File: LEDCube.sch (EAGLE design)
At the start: 19 parts

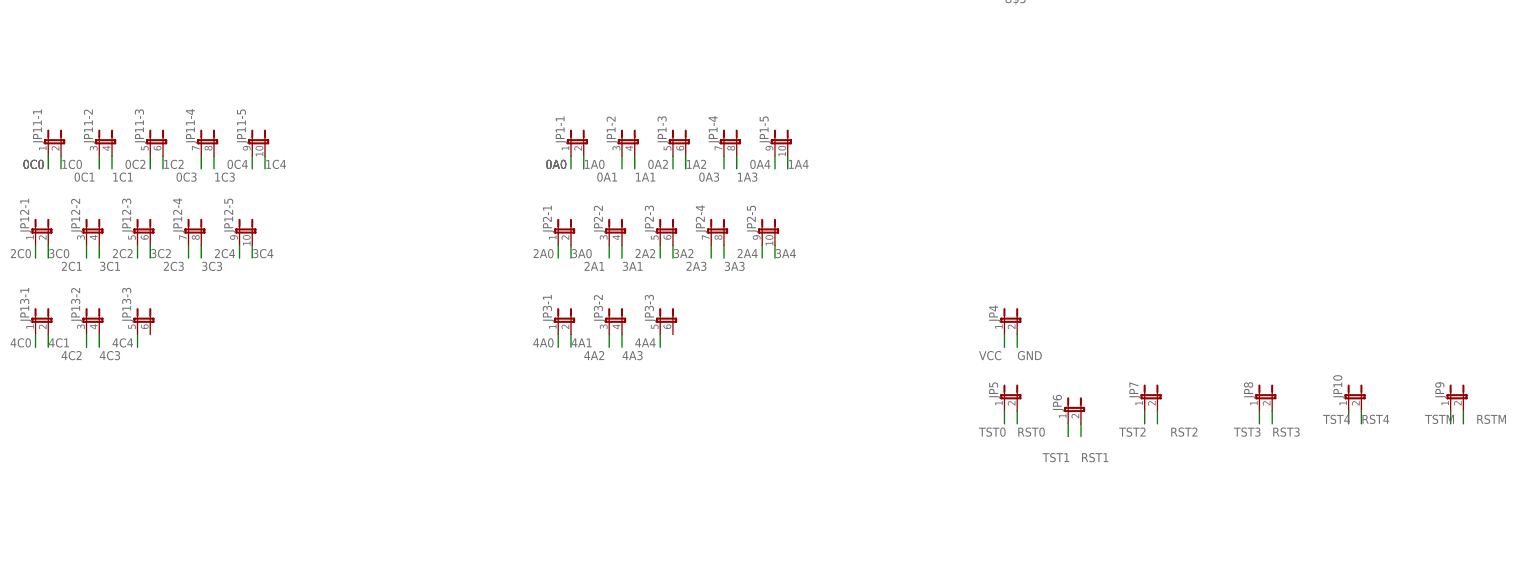
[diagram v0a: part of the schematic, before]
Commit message: Laid out MSP430 board. Not routed yet.
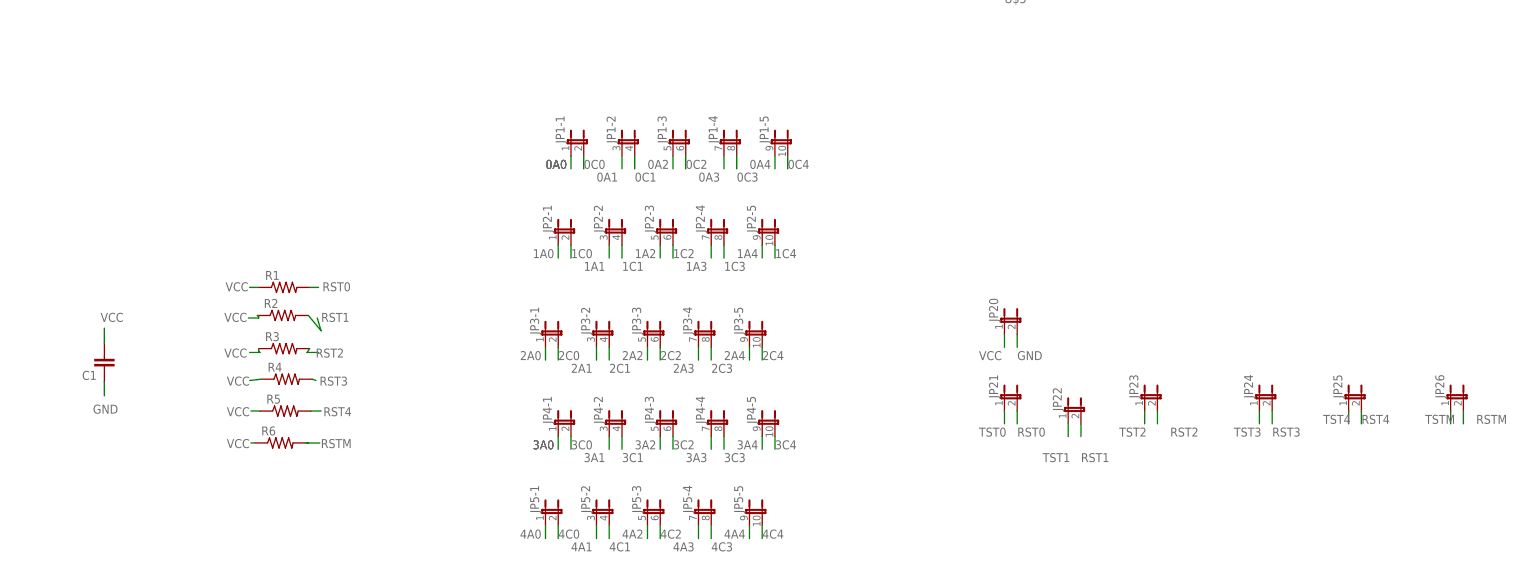
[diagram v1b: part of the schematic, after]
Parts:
- removed JP11, JP12, JP13: (no value), jumper:JP5QE
- added C1: (no value), eagle-ltspice:CC1206
- added JP20, JP21: (no value), jumper:JP1E
- added R1, R2, R3, R4, R5, R6: (no value), rcl:R-US_R1206
- JP4, JP5: device jumper:JP1E -> jumper:JP5QE
- renumbered JP10 to JP25, JP6 to JP22, JP7 to JP23, JP8 to JP24, JP9 to JP26
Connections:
- net 0C0: now also JP1-1.2; no longer JP11-1.1
- net 0C1: now also JP1-2.2; no longer JP11-2.1
- net 0C2: now also JP1-3.2; no longer JP11-3.1
- net 0C3: now also JP1-4.2; no longer JP11-4.1
- net 0C4: now also JP1-5.2; no longer JP11-5.1
- net 1A0: now also JP2-1.1; no longer JP1-1.2
- net 1A1: now also JP2-2.1; no longer JP1-2.2
- net 1A2: now also JP2-3.1; no longer JP1-3.2
- net 1A3: now also JP2-4.1; no longer JP1-4.2
- net 1A4: now also JP2-5.1; no longer JP1-5.2
- net 1C0: now also JP2-1.2; no longer JP11-1.2
- net 1C1: now also JP2-2.2; no longer JP11-2.2
- net 1C2: now also JP2-3.2; no longer JP11-3.2
- net 1C3: now also JP2-4.2; no longer JP11-4.2
- net 1C4: now also JP2-5.2; no longer JP11-5.2
- net 2A0: now also JP3-1.1; no longer JP2-1.1
- net 2A1: now also JP3-2.1; no longer JP2-2.1
- net 2A2: now also JP3-3.1; no longer JP2-3.1
- net 2A3: now also JP3-4.1; no longer JP2-4.1
- net 2A4: now also JP3-5.1; no longer JP2-5.1
- net 2C0: now also JP3-1.2; no longer JP12-1.1
- net 2C1: now also JP3-2.2; no longer JP12-2.1
- net 2C2: now also JP3-3.2; no longer JP12-3.1
- net 2C3: now also JP3-4.2; no longer JP12-4.1
- net 2C4: now also JP3-5.2; no longer JP12-5.1
- net 3A0: now also JP4-1.1; no longer JP2-1.2
- net 3A1: now also JP4-2.1; no longer JP2-2.2
- net 3A2: now also JP4-3.1; no longer JP2-3.2
- net 3A3: now also JP4-4.1; no longer JP2-4.2
- net 3A4: now also JP4-5.1; no longer JP2-5.2
- net 3C0: now also JP4-1.2; no longer JP12-1.2
- net 3C1: now also JP4-2.2; no longer JP12-2.2
- net 3C2: now also JP4-3.2; no longer JP12-3.2
- net 3C3: now also JP4-4.2; no longer JP12-4.2
- net 3C4: now also JP4-5.2; no longer JP12-5.2
- net 4A0: now also JP5-1.1; no longer JP3-1.1
- net 4A1: now also JP5-2.1; no longer JP3-1.2
- net 4A2: now also JP5-3.1; no longer JP3-2.1
- net 4A3: now also JP5-4.1; no longer JP3-2.2
- net 4A4: now also JP5-5.1; no longer JP3-3.1
- net 4C0: now also JP5-1.2; no longer JP13-1.1
- net 4C1: now also JP5-2.2; no longer JP13-1.2
- net 4C2: now also JP5-3.2; no longer JP13-2.1
- net 4C3: now also JP5-4.2; no longer JP13-2.2
- net 4C4: now also JP5-5.2; no longer JP13-3.1
- net GND: now also C1.1, JP20.2; no longer JP4.2
- net RST0: now also JP21.2, R1.2; no longer JP5.2
- net RST1: now also R2.2
- net RST2: now also R3.2
- net RST3: now also R4.2
- net RST4: now also R5.2
- net RSTM: now also R6.2
- net TST0: now also JP21.1; no longer JP5.1
- net VCC: now also C1.2, JP20.1, R1.1, R2.1, R3.1, R4.1, R5.1, R6.1; no longer JP4.1
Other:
- moved on the sheet: JP3-1, JP3-2, JP3-3
